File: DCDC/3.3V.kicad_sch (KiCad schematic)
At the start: 26 parts, among them J9 GND, M1-2 30V 60A, M2-2 30V 35A

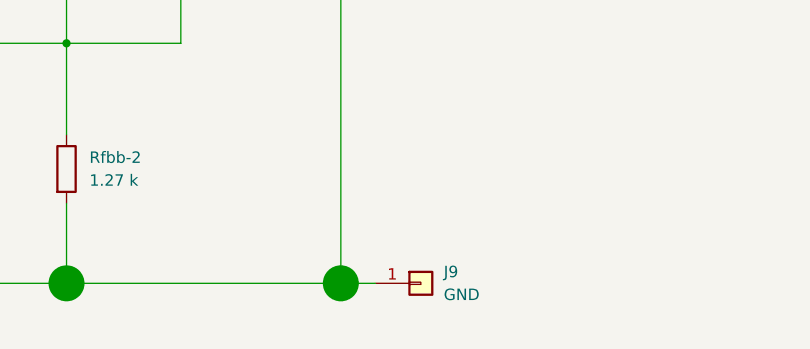
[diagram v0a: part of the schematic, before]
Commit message: pcb updated with all parts
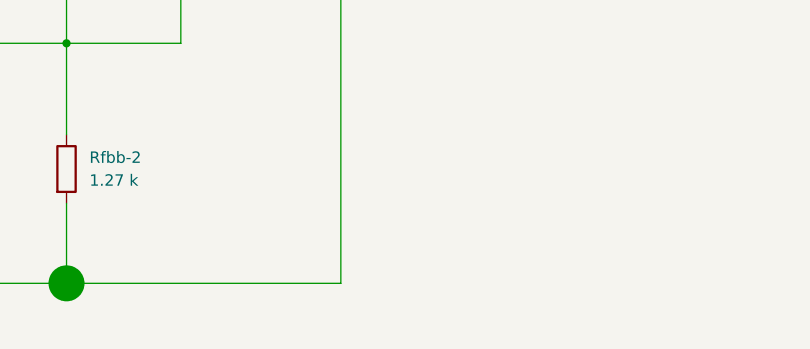
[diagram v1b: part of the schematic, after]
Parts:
- removed J9: GND, Connector_Pin:Pin_D1.4mm_L8.5mm_W2.8mm_FlatFork, symbol Connector_Generic:Conn_01x01
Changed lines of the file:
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@@
   (junction (at 60.96 21.59) (diameter 4) (color 0 0 0 0)
   )
-  (junction (at 223.52 154.94) (diameter 4) (color 0 0 0 0)
-  )
   (junction (at 54.61 21.59) (diameter 4) (color 0 0 0 0)
   )
@@
   )
   (wire (pts (xy 153.67 87.63) (xy 153.67 124.46))
-    (stroke (width 0) (type default))
-  )
-  (wire (pts (xy 223.52 154.94) (xy 227.33 154.94))
     (stroke (width 0) (type default))
   )
@@
         )
       )
-    )
-  )
-  (symbol (lib_id "Connector_Generic:Conn_01x01") (at 232.41 154.94 0) (unit 1)
-    (in_bom yes) (on_board yes) (dnp no) (fields_autoplaced)
-    (property "Reference" "J9" (at 234.95 153.67 0)
-      (effects (font (size 1.27 1.27)) (justify left))
-    )
-    (property "Value" "GND" (at 234.95 156.21 0)
-      (effects (font (size 1.27 1.27)) (justify left))
-    )
-    (property "Footprint" "Connector_Pin:Pin_D1.4mm_L8.5mm_W2.8mm_FlatFork" (at 232.41 154.94 0)
-      (effects (font (size 1.27 1.27)) hide)
-    )
-    (property "Datasheet" "~" (at 232.41 154.94 0)
-      (effects (font (size 1.27 1.27)) hide)
-    )
-    (property "Sim.Enable" "0" (at 232.41 154.94 0)
-      (effects (font (size 1.27 1.27)) hide)
-    )
-    (pin "1")
-    (instances
-      (project "dcdc3"
-        (path "/074a9d0b-fc12-4aa8-94e4-356d74449fb4/422f6745-5801-4eed-ad16-242ed2cec958"
-          (reference "J9") (unit 1)
-        )
-      )

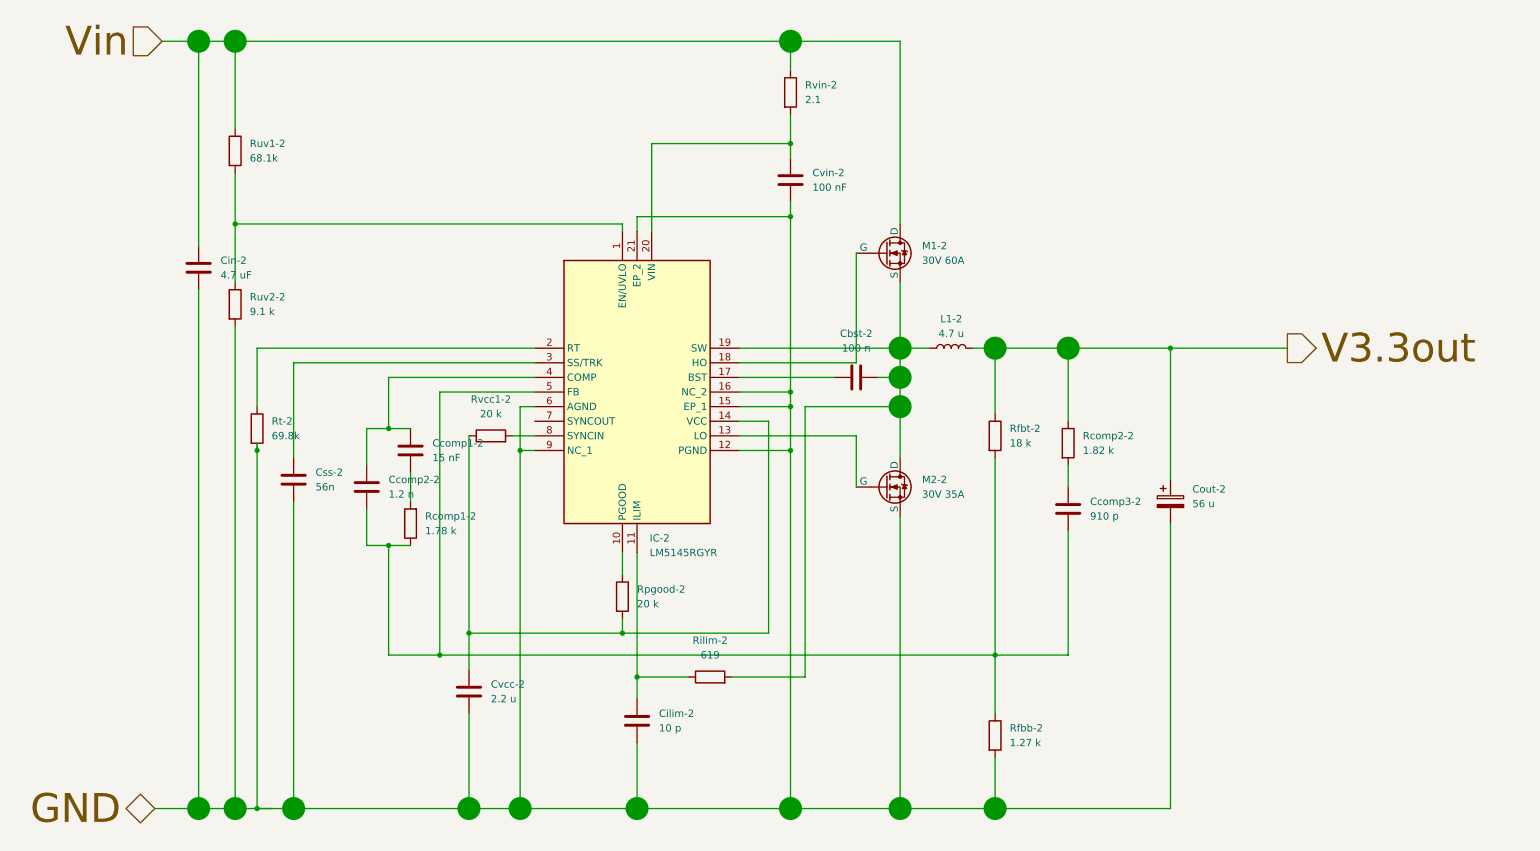
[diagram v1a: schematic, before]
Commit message: pcb designed for 3 outputs
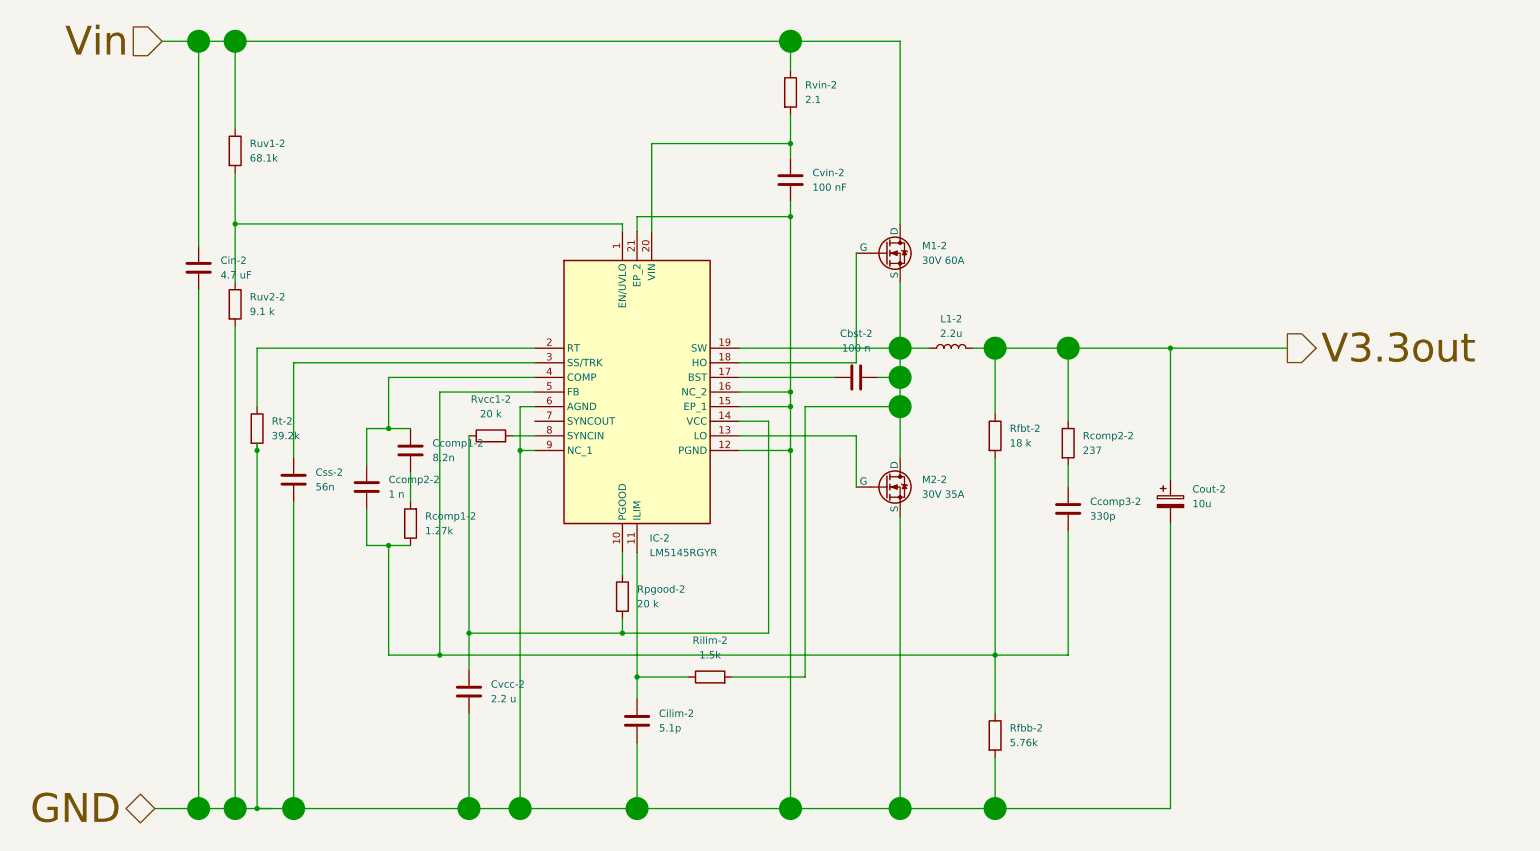
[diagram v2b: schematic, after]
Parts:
- Ccomp1-2: value 15 nF -> 8.2n; Manufacturer_Part_Number GRM155R71C153KA01D -> GRM155R71C822KA01D
- Ccomp2-2: value 1.2 n -> 1 n; Manufacturer_Part_Number GRM155R71H122KA01D -> GRM155R71C102KA01D
- Ccomp3-2: value 910 p -> 330p; Manufacturer_Part_Number GRM1555C1H911JA01D -> CGA2B2X7R1H331K050BA
- Cilim-2: value 10 p -> 5.1p; footprint Capacitor_SMD:C_0603_1608Metric -> Capacitor_SMD:C_0805_2012Metric; Manufacturer_Part_Number GRM1885C2A100JA01D -> GQM2195C2A5R1CB01D
- Cout-2: value 56 u -> 10u; Manufacturer_Part_Number APSG250ELL560MF05S -> VDC: 10 V ESR: 8 mΩ
- IC-2: footprint Library:RGY0020B -> RGY0020B
- L1-2: value 4.7 u -> 2.2u; Manufacturer_Part_Number R=15,L=2.145,N=11,d=1.95, Rwire=1.68 mOhm -> (none)
- Rcomp1-2: value 1.78 k -> 1.27k; Manufacturer_Part_Number CRCW04021K78FKED -> CRCW04021K27FKED
- Rcomp2-2: value 1.82 k -> 237; Manufacturer_Part_Number CRCW04021K82FKED -> CRCW0402237RFKED
- Rfbb-2: value 1.27 k -> 5.76k; Manufacturer_Part_Number CRCW04021K27FKED -> CRCW04025K76FKED
- Rilim-2: value 619 -> 1.5k; Manufacturer_Part_Number CRCW0402619RFKED -> CRCW04021K50FKED
- Rt-2: value 69.8k -> 39.2k; Manufacturer_Part_Number CRCW040269K8FKED -> CRCW040239K2FKED
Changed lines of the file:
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@@
       (effects (font (size 1.27 1.27)) (justify left))
     )
-    (property "Footprint" "Library:RGY0020B" (at 144.78 157.15 0)
+    (property "Footprint" "RGY0020B" (at 144.78 157.15 0)
       (effects (font (size 1.27 1.27)) (justify left top) hide)
     )
@@
       (effects (font (size 1.27 1.27)) (justify left))
     )
-    (property "Value" "56 u" (at 227.33 101.981 0)
+    (property "Value" "10u" (at 227.33 101.981 0)
       (effects (font (size 1.27 1.27)) (justify left))
     )
@@
       (effects (font (size 1.27 1.27)) hide)
     )
-    (property "Datasheet" "https://hu.mouser.com/datasheet/2/420/PSGLL_e-2507380.pdf" (at 223.52 101.6 0)
-      (effects (font (size 1.27 1.27)) hide)
-    )
-    (property "Manufacturer_Part_Number" "APSG250ELL560MF05S" (at 223.52 101.6 0)
+    (property "Datasheet" "~" (at 223.52 101.6 0)
+      (effects (font (size 1.27 1.27)) hide)
+    )
+    (property "Manufacturer_Part_Number" "VDC: 10 V  ESR: 8 mΩ" (at 223.52 101.6 0)
       (effects (font (size 1.27 1.27)) hide)
     )
@@
       (effects (font (size 1.27 1.27)) (justify right))
     )
-    (property "Value" "1.78 k" (at 93.98 106.68 0)
+    (property "Value" "1.27k" (at 93.98 106.68 0)
       (effects (font (size 1.27 1.27)) (justify right))
     )
@@
       (effects (font (size 1.27 1.27)) hide)
     )
-    (property "Manufacturer_Part_Number" "CRCW04021K78FKED" (at 91.44 105.41 0)
+    (property "Manufacturer_Part_Number" "CRCW04021K27FKED" (at 91.44 105.41 0)
       (effects (font (size 1.27 1.27)) hide)
     )
@@
       (effects (font (size 1.27 1.27)) (justify left))
     )
-    (property "Value" "910 p" (at 209.55 104.14 0)
+    (property "Value" "330p" (at 209.55 104.14 0)
       (effects (font (size 1.27 1.27)) (justify left))
     )
@@
       (effects (font (size 1.27 1.27)) hide)
     )
-    (property "Manufacturer_Part_Number" "GRM1555C1H911JA01D" (at 205.74 102.87 0)
+    (property "Manufacturer_Part_Number" "CGA2B2X7R1H331K050BA" (at 205.74 102.87 0)
       (effects (font (size 1.27 1.27)) hide)
     )
@@
       (effects (font (size 1.27 1.27)))
     )
-    (property "Value" "4.7 u" (at 185.42 72.39 90)
+    (property "Value" "2.2u" (at 185.42 72.39 90)
       (effects (font (size 1.27 1.27)))
     )
@@
       (effects (font (size 1.27 1.27)) hide)
     )
-    (property "Datasheet" "https://www.allaboutcircuits.com/tools/coil-inductance-calculator/" (at 185.42 74.93 0)
-      (effects (font (size 1.27 1.27)) hide)
-    )
-    (property "Manufacturer_Part_Number" "R=15,L=2.145,N=11,d=1.95, Rwire=1.68 mOhm" (at 185.42 74.93 0)
+    (property "Datasheet" "~" (at 185.42 74.93 0)
+      (effects (font (size 1.27 1.27)) hide)
+    )
+    (property "Manufacturer_Part_Number" "" (at 185.42 74.93 0)
       (effects (font (size 1.27 1.27)) hide)
     )
@@
       (effects (font (size 1.27 1.27)) hide)
     )
-    (property "Datasheet" "https://hu.mouser.com/datasheet/2/240/media-3320211.pdf" (at 173.99 71.12 0)
+    (property "Datasheet" "https://ngspice.sourceforge.io/docs/ngspice-manual.pdf" (at 173.99 71.12 0)
       (effects (font (size 1.27 1.27)) hide)
     )
@@
       (effects (font (size 1.27 1.27)) (justify left))
     )
-    (property "Value" "1.82 k" (at 208.28 92.71 0)
+    (property "Value" "237" (at 208.28 92.71 0)
       (effects (font (size 1.27 1.27)) (justify left))
     )
@@
       (effects (font (size 1.27 1.27)) hide)
     )
-    (property "Manufacturer_Part_Number" "CRCW04021K82FKED" (at 205.74 91.44 0)
+    (property "Manufacturer_Part_Number" "CRCW0402237RFKED" (at 205.74 91.44 0)
       (effects (font (size 1.27 1.27)) hide)
     )
@@
       (effects (font (size 1.27 1.27)) (justify left))
     )
-    (property "Value" "10 p" (at 134.62 140.97 0)
-      (effects (font (size 1.27 1.27)) (justify left))
-    )
-    (property "Footprint" "Capacitor_SMD:C_0603_1608Metric" (at 131.7752 143.51 0)
+    (property "Value" "5.1p" (at 134.62 140.97 0)
+      (effects (font (size 1.27 1.27)) (justify left))
+    )
+    (property "Footprint" "Capacitor_SMD:C_0805_2012Metric" (at 131.7752 143.51 0)
       (effects (font (size 1.27 1.27)) hide)
     )
@@
       (effects (font (size 1.27 1.27)) hide)
     )
-    (property "Manufacturer_Part_Number" "GRM1885C2A100JA01D" (at 130.81 139.7 0)
+    (property "Manufacturer_Part_Number" "GQM2195C2A5R1CB01D" (at 130.81 139.7 0)
       (effects (font (size 1.27 1.27)) hide)
     )
@@
       (effects (font (size 1.27 1.27)) (justify left))
     )
-    (property "Value" "69.8k" (at 67.31 90.17 0)
+    (property "Value" "39.2k" (at 67.31 90.17 0)
       (effects (font (size 1.27 1.27)) (justify left))
     )
@@
       (effects (font (size 1.27 1.27)) hide)
     )
-    (property "Manufacturer_Part_Number" "CRCW040269K8FKED" (at 64.77 88.9 0)
+    (property "Manufacturer_Part_Number" "CRCW040239K2FKED" (at 64.77 88.9 0)
       (effects (font (size 1.27 1.27)) hide)
     )
@@
       (effects (font (size 1.27 1.27)) (justify left))
     )
-    (property "Value" "1.27 k" (at 195.58 143.51 0)
+    (property "Value" "5.76k" (at 195.58 143.51 0)
       (effects (font (size 1.27 1.27)) (justify left))
     )
@@
       (effects (font (size 1.27 1.27)) hide)
     )
-    (property "Manufacturer_Part_Number" "CRCW04021K27FKED" (at 193.04 142.24 0)
+    (property "Manufacturer_Part_Number" "CRCW04025K76FKED" (at 193.04 142.24 0)
       (effects (font (size 1.27 1.27)) hide)
     )
@@
       (effects (font (size 1.27 1.27)) (justify right))
     )
-    (property "Value" "15 nF" (at 95.25 93.98 0)
+    (property "Value" "8.2n" (at 95.25 93.98 0)
       (effects (font (size 1.27 1.27)) (justify right))
     )
@@
       (effects (font (size 1.27 1.27)) hide)
     )
-    (property "Manufacturer_Part_Number" "GRM155R71C153KA01D" (at 91.44 92.71 0)
+    (property "Manufacturer_Part_Number" "GRM155R71C822KA01D" (at 91.44 92.71 0)
       (effects (font (size 1.27 1.27)) hide)
     )
@@
       (effects (font (size 1.27 1.27)) (justify right))
     )
-    (property "Value" "1.2 n" (at 87.63 100.33 0)
+    (property "Value" "1 n" (at 87.63 100.33 0)
       (effects (font (size 1.27 1.27)) (justify right))
     )
@@
       (effects (font (size 1.27 1.27)) hide)
     )
-    (property "Manufacturer_Part_Number" "GRM155R71H122KA01D" (at 83.82 99.06 0)
+    (property "Manufacturer_Part_Number" "GRM155R71C102KA01D" (at 83.82 99.06 0)
       (effects (font (size 1.27 1.27)) hide)
     )
@@
       (effects (font (size 1.27 1.27)))
     )
-    (property "Value" "619" (at 143.51 128.27 90)
+    (property "Value" "1.5k" (at 143.51 128.27 90)
       (effects (font (size 1.27 1.27)))
     )
@@
       (effects (font (size 1.27 1.27)) hide)
     )
-    (property "Manufacturer_Part_Number" "CRCW0402619RFKED" (at 143.51 132.08 0)
-      (effects (font (size 1.27 1.27)) hide)
-    )
+    (property "Manufacturer_Part_Number" "CRCW04021K50FKED" (at 143.51 132.08 0)
+      (effects (font (size 1.27 1.27)) hide)
+    )

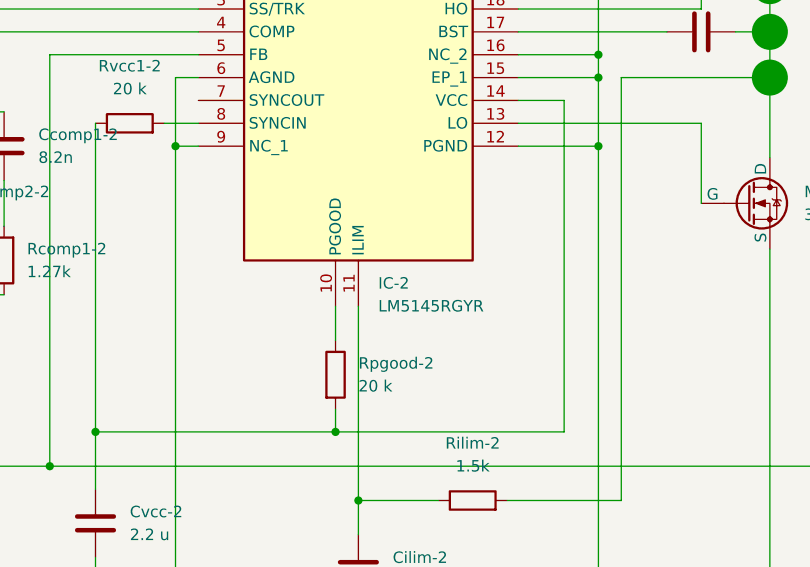
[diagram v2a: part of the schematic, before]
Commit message: dcdc simulation, mechanical drawings
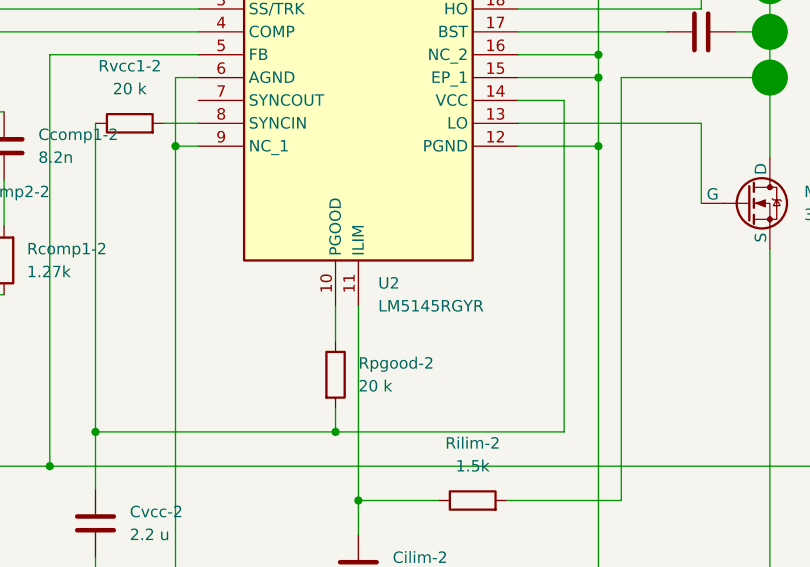
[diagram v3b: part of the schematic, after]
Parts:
- renumbered IC-2 to U2

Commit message: one module of the dcdc converter seems ready again...
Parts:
- removed M1-2: 30V 60A, Library:TO545P521X1594X2566-3P, symbol Simulation_SPICE:NMOS
- removed M2-2: 30V 35A, Library:TO545P521X1594X2566-3P, symbol Simulation_SPICE:NMOS
- added M1-2: 30V 60A, Library:TO545P521X1594X2566-3P, symbol Local:IXFX360N10T
- added M2-2: 30V 35A, Library:TO545P521X1594X2566-3P, symbol Local:IXFX360N10T
- U2: footprint RGY0020B -> Library:RGY0020B
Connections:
- net GND: now also M2-2.3
- net Vin: now also M1-2.2
- net at U2.13 (LO): now also M2-2.1
- net at U2.18 (HO): now also M1-2.1
- net at Cbst-2.2, L1-2.1, Rilim-2.2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: now also M1-2.3, M2-2.2

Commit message: 3 modules of DCDC, hinge
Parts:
- L1-2: Manufacturer_Part_Number (none) -> D=15mm,N=10,L=20mm,d=2mm
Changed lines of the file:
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@@
 			)
 		)
-		(property "Datasheet" "~"
+		(property "Datasheet" "https://www.allaboutcircuits.com/tools/coil-inductance-calculator/"
 			(at 185.42 74.93 0)
 			(effects
@@
 			)
 		)
-		(property "Manufacturer_Part_Number" ""
+		(property "Manufacturer_Part_Number" "D=15mm,N=10,L=20mm,d=2mm"
 			(at 185.42 74.93 0)
 			(effects

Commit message: DCDC fix unavailable parts, BMS redesign, handle fix, rearrange top half
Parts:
- Cbst-2: Manufacturer_Part_Number GRM188R61E104KA01D -> C0603C104J1RACAUTO
- Cilim-2: Manufacturer_Part_Number GQM2195C2A5R1CB01D -> C0805C519DBGACTU
- Cout-2: footprint Capacitor_THT:C_Radial_D6.3mm_H5.0mm_P2.50mm -> Capacitor_THT:C_Radial_D10.0mm_H12.5mm_P5.00mm; Manufacturer_Part_Number VDC: 10 V ESR: 8 mΩ -> KTD500B106M55A0T00
- Ruv1-2: footprint Resistor_SMD:R_0201_0603Metric -> Resistor_SMD:R_0603_1608Metric; Manufacturer_Part_Number RC0201FR-7D68K1L -> ERA-3VEB6812V
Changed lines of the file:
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@@
 			)
 		)
-		(property "Footprint" "Capacitor_THT:C_Radial_D6.3mm_H5.0mm_P2.50mm"
+		(property "Footprint" "Capacitor_THT:C_Radial_D10.0mm_H12.5mm_P5.00mm"
 			(at 224.4852 105.41 0)
 			(effects
@@
 			)
 		)
-		(property "Manufacturer_Part_Number" "VDC: 10 V  ESR: 8 mΩ"
+		(property "Manufacturer_Part_Number" "KTD500B106M55A0T00 "
 			(at 223.52 101.6 0)
 			(effects
@@
 			)
 		)
-		(property "Manufacturer_Part_Number" "GRM188R61E104KA01D"
+		(property "Manufacturer_Part_Number" "C0603C104J1RACAUTO"
 			(at 168.91 80.01 0)
 			(effects
@@
 			)
 		)
-		(property "Manufacturer_Part_Number" "GQM2195C2A5R1CB01D"
+		(property "Manufacturer_Part_Number" "C0805C519DBGACTU"
 			(at 130.81 139.7 0)
 			(effects
@@
 			)
 		)
-		(property "Footprint" "Resistor_SMD:R_0201_0603Metric"
+		(property "Footprint" "Resistor_SMD:R_0603_1608Metric"
 			(at 59.182 40.64 90)
 			(effects
@@
 			)
 		)
-		(property "Datasheet" "~"
+		(property "Datasheet" ""
 			(at 60.96 40.64 0)
 			(effects
@@
 			)
 		)
-		(property "Manufacturer_Part_Number" "RC0201FR-7D68K1L"
+		(property "Manufacturer_Part_Number" "ERA-3VEB6812V"
 			(at 60.96 40.64 0)
 			(effects

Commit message: coil redesign, materials
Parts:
- L1-2: Manufacturer_Part_Number D=15mm,N=10,L=20mm,d=2mm -> D=21mm,N=7,L=7.9mm,d=1.12mm
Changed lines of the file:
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@@
 			)
 		)
-		(property "Manufacturer_Part_Number" "D=15mm,N=10,L=20mm,d=2mm"
+		(property "Manufacturer_Part_Number" "D=21mm,N=7,L=7.9mm,d=1.12mm"
 			(at 185.42 74.93 0)
 			(effects
